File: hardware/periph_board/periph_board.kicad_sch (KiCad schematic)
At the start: 25 parts, among them IC100 CD74HC4067SM96, IC101 LM2937ET-3.3_NOPB, IC102 ADC121S021CIMFX_NOPB, J100 2x10 Male Pins

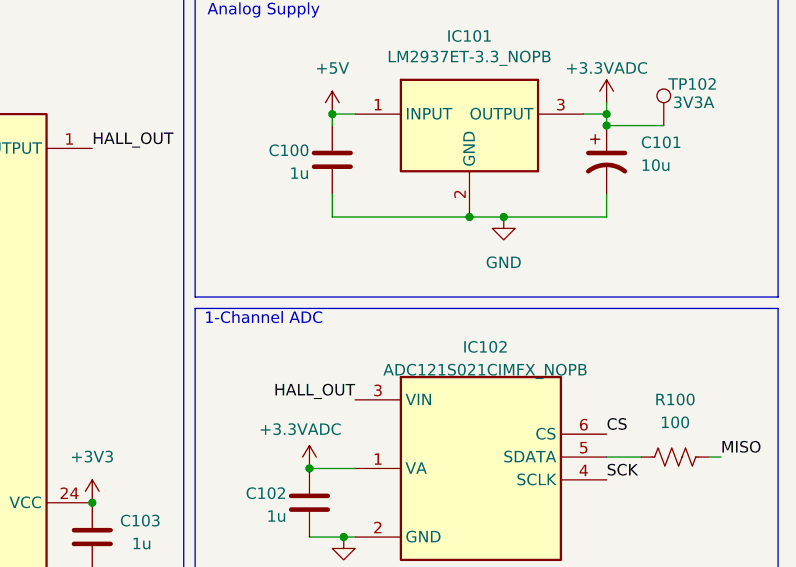
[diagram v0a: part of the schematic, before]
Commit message: fixed sides of peripheral board not being symmetrical. added teardrops. name of board tbd
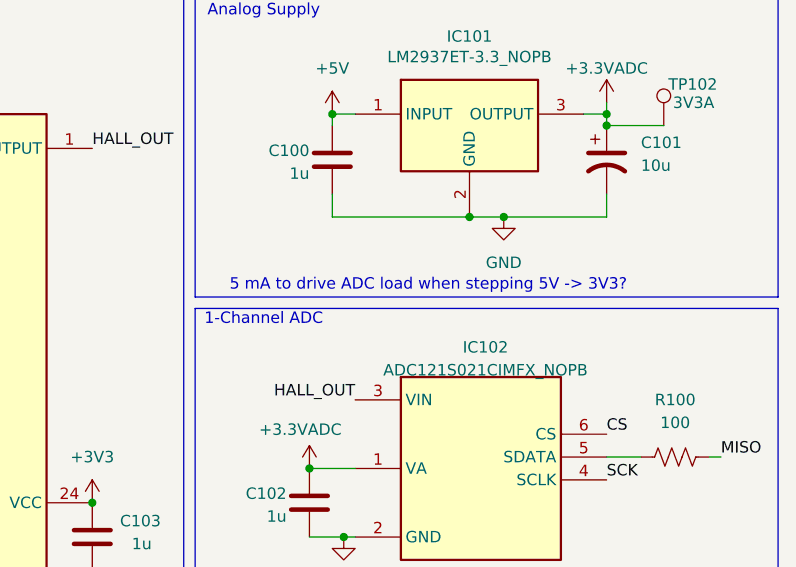
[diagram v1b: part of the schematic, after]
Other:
- note added: "5 mA to drive ADC load when stepping 5V -> 3V3?"
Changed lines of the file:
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@@
+		)
+	)
+	(text "5 mA to drive ADC load when stepping 5V -> 3V3?"
+		(exclude_from_sim no)
+		(at 217.678 46.99 0)
+		(effects
+			(font
+				(size 1.27 1.27)
+			)
 		)
 	)

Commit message: drew schematic
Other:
- note added: "1.2 mA worst case scenario"
- note added: "10 mA worst case scenario"
- note removed: "20 mA worst case scenario"
- note removed: "5 mA to drive ADC load when stepping 5V -> 3V3?"
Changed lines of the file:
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@@
 		)
 	)
-	(text "20 mA worst case scenario"
+	(text "1.2 mA worst case scenario"
 		(exclude_from_sim no)
 		(at 205.74 82.55 0)
@@
 		)
 	)
-	(text "5 mA to drive ADC load when stepping 5V -> 3V3?"
+	(text "10 mA worst case scenario"
 		(exclude_from_sim no)
-		(at 217.678 46.99 0)
+		(at 205.74 47.244 0)
 		(effects
 			(font
@@
 		)
 		(property "Value" "ADC121S021CIMFX_NOPB"
-			(at 224.028 56.388 0)
+			(at 223.52 55.626 0)
 			(effects
 				(font

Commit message: save before nuke SPI ADC
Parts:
- added R200: 3k, Resistor_SMD:R_0805_2012Metric, symbol Device:R_Small_US
- added R201: 3k3, Resistor_SMD:R_0805_2012Metric, symbol Device:R_Small_US
- added R202: 7k5, Resistor_SMD:R_0805_2012Metric, symbol Device:R_Small_US
- added R203: 9k1, Resistor_SMD:R_0805_2012Metric, symbol Device:R_Small_US
- added R204: 1k5, Resistor_SMD:R_0805_2012Metric, symbol Device:R_Small_US
- added R205: 1k3, Resistor_SMD:R_0805_2012Metric, symbol Device:R_Small_US
- added R206: 2k, Resistor_SMD:R_0805_2012Metric, symbol Device:R_Small_US
- added R207: 2k0, Resistor_SMD:R_0805_2012Metric, symbol Device:R_Small_US
- J100: value 2x10 Male Pins -> 2x9 Male Pins; footprint Connector_PinSocket_2.54mm:PinSocket_2x10_P2.54mm_Vertical -> Connector_PinSocket_2.54mm:PinSocket_2x09_P2.54mm_Vertical; symbol Connector_Generic:Conn_02x10_Odd_Even -> Connector_Generic:Conn_02x09_Odd_Even
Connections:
- net +3.3VADC is gone; now on net +3V3: C101.1, C102.2, IC101.3 (OUTPUT), IC102.1 (VA), TP102.1
- net +3V3: now also R200.1, R202.1, R204.1, R205.1; no longer J100.1 (Pin_1), J100.2 (Pin_2)
- net +5V: now also J100.1 (Pin_1), J100.2 (Pin_2); no longer J100.3 (Pin_3), J100.4 (Pin_4)
- net CS: now also J100.7 (Pin_7), J100.8 (Pin_8); no longer J100.10 (Pin_10), J100.9 (Pin_9)
- net GND: now also J100.17 (Pin_17), J100.18 (Pin_18), R201.2, R203.2, R206.2, R207.2; no longer J100.19 (Pin_19), J100.20 (Pin_20)
- net MISO: now also J100.5 (Pin_5), J100.6 (Pin_6); no longer J100.7 (Pin_7), J100.8 (Pin_8)
- net S0: now also J100.10 (Pin_10), J100.9 (Pin_9); no longer J100.11 (Pin_11), J100.12 (Pin_12)
- net S1: now also J100.11 (Pin_11), J100.12 (Pin_12); no longer J100.13 (Pin_13), J100.14 (Pin_14)
- net S2: now also J100.13 (Pin_13), J100.14 (Pin_14); no longer J100.15 (Pin_15), J100.16 (Pin_16)
- net S3: now also J100.15 (Pin_15), J100.16 (Pin_16); no longer J100.17 (Pin_17), J100.18 (Pin_18)
- net SCK: now also J100.3 (Pin_3), J100.4 (Pin_4); no longer J100.5 (Pin_5), J100.6 (Pin_6)
- net 2V000: now reaches IC100.16 (I15)
- net 2V000: now also R205.2, R207.1
- net 1V866: now reaches IC100.17 (I14)
- net 1V866: now also R204.2, R206.1
- net 1V810: now reaches IC100.18 (I13)
- net 1V810: now also R202.2, R203.1
- net 1V729: now reaches IC100.19 (I12)
- net 1V729: now also R200.2, R201.1
- no-connect marks 4 -> 0
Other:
- note added: "Test Voltages"
- moved on the sheet: C100, C101, C102, C103, H100, H101, IC100, IC101, IC102, R100, TP102

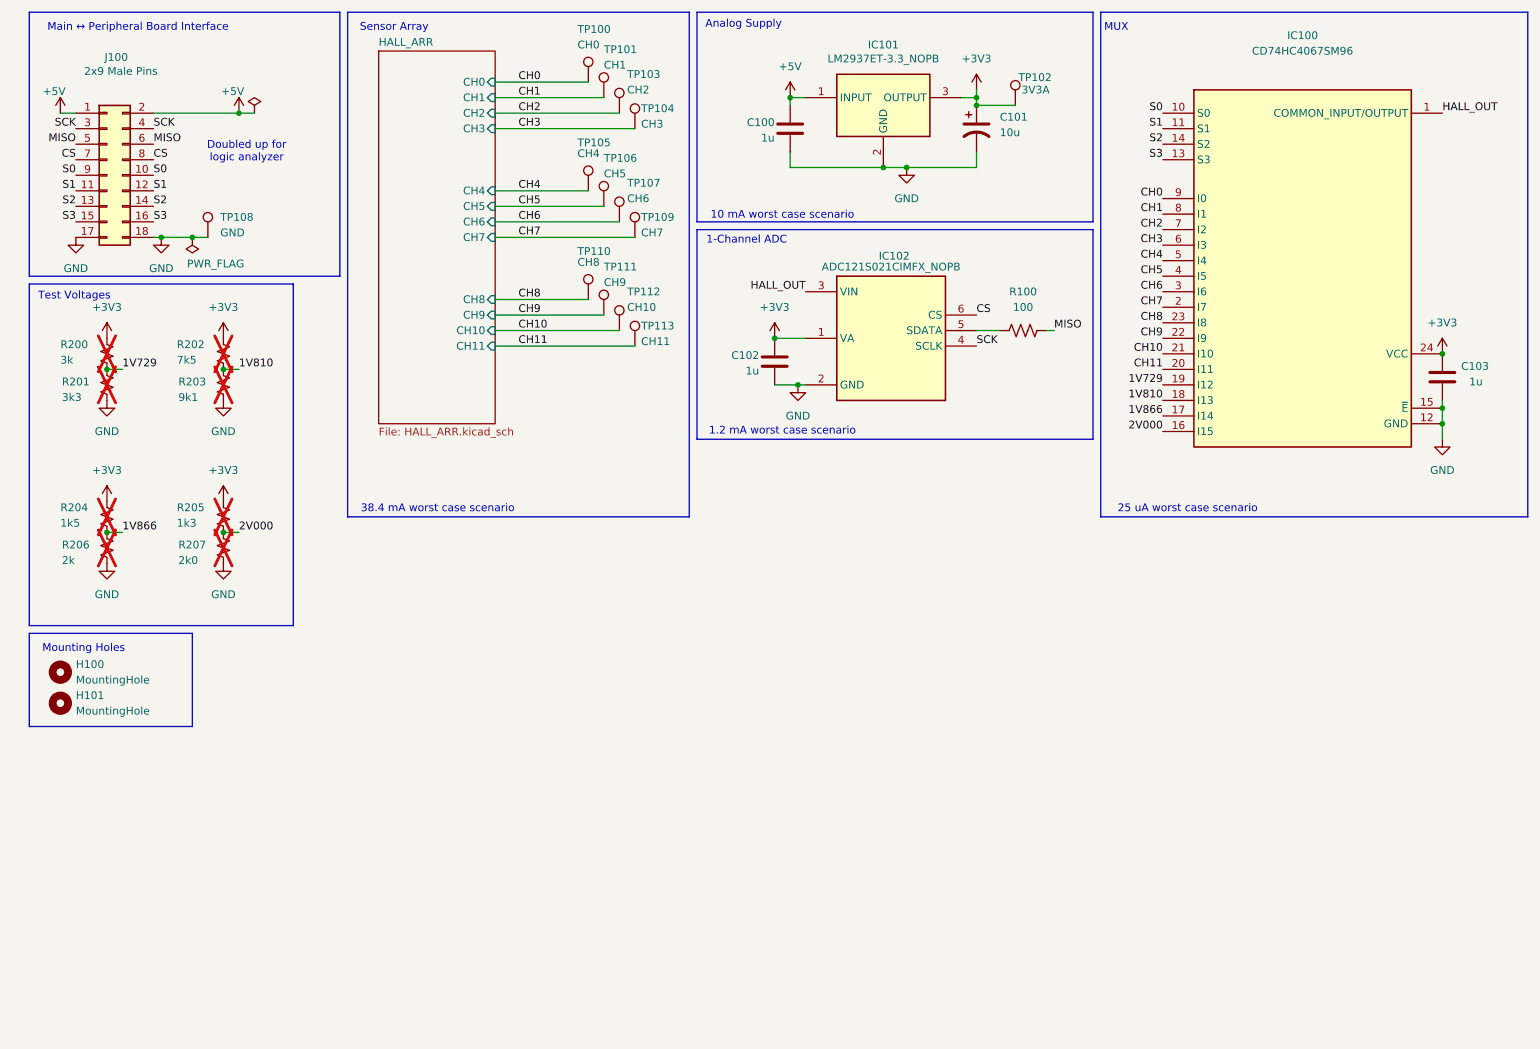
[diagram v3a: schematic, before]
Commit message: port to i2c for both boards. periph board passes drc
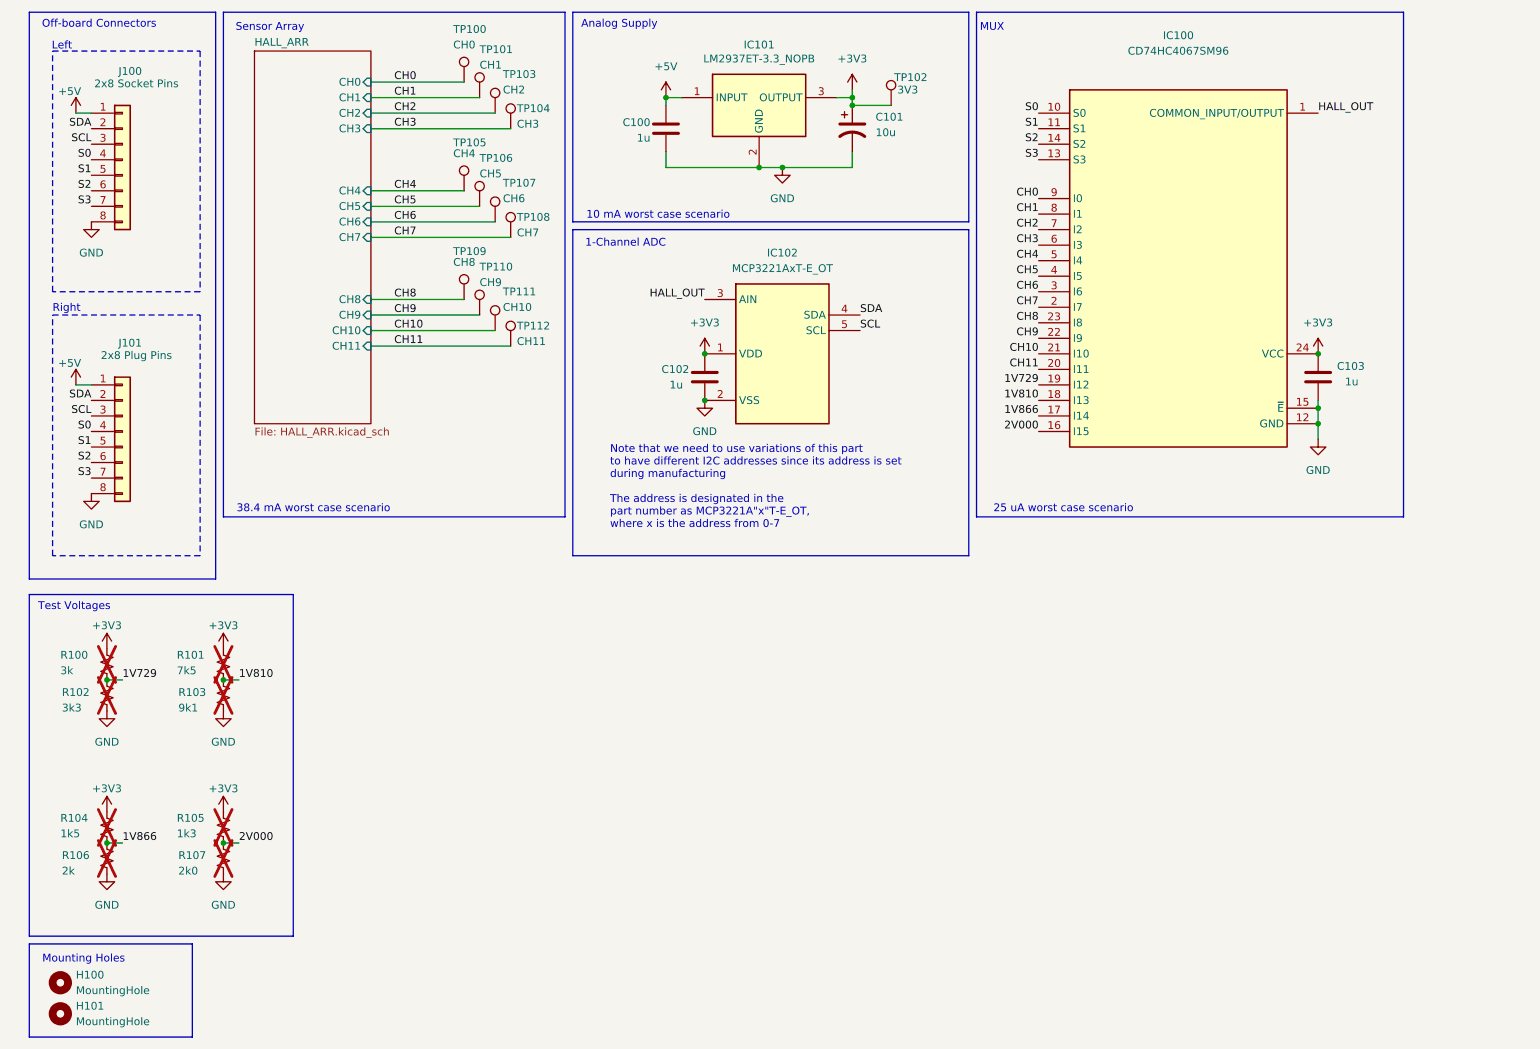
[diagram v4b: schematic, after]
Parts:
- removed IC102: ADC121S021CIMFX_NOPB, SamacSys_Parts:SOT95P280X145-6N, symbol SamacSys_Parts:ADC121S021CIMFX_NOPB
- removed R100: 100, Resistor_SMD:R_0805_2012Metric, symbol Device:R_US
- removed TP108: GND, SamacSys_Parts:bettertestpoint2, symbol Connector:TestPoint
- added IC102: MCP3221AxT-E_OT, SOT95P280X145-5N, symbol SamacSys_Parts:MCP3221A5T-E_OT
- added J101: 2x8 Plug Pins, Connector_PinSocket_2.54mm:PinSocket_1x08_P2.54mm_Vertical, symbol Connector_Generic:Conn_01x08
- C101: footprint Capacitor_SMD:C_0805_2012Metric -> Capacitor_SMD:C_0805_2012Metric_Pad1.18x1.45mm_HandSolder
- J100: value 2x9 Male Pins -> 2x8 Socket Pins; footprint Connector_PinSocket_2.54mm:PinSocket_2x09_P2.54mm_Vertical -> Connector_PinSocket_2.54mm:PinSocket_1x08_P2.54mm_Vertical; symbol Connector_Generic:Conn_02x09_Odd_Even -> Connector_Generic:Conn_01x08
- R100: renamed from R200; footprint Resistor_SMD:R_0805_2012Metric -> Resistor_SMD:R_0805_2012Metric_Pad1.20x1.40mm_HandSolder
- R101: renamed from R202; footprint Resistor_SMD:R_0805_2012Metric -> Resistor_SMD:R_0805_2012Metric_Pad1.20x1.40mm_HandSolder
- R102: renamed from R201; footprint Resistor_SMD:R_0805_2012Metric -> Resistor_SMD:R_0805_2012Metric_Pad1.20x1.40mm_HandSolder
- R103: renamed from R203; footprint Resistor_SMD:R_0805_2012Metric -> Resistor_SMD:R_0805_2012Metric_Pad1.20x1.40mm_HandSolder
- R104: renamed from R204; footprint Resistor_SMD:R_0805_2012Metric -> Resistor_SMD:R_0805_2012Metric_Pad1.20x1.40mm_HandSolder
- R105: renamed from R205; footprint Resistor_SMD:R_0805_2012Metric -> Resistor_SMD:R_0805_2012Metric_Pad1.20x1.40mm_HandSolder
- R106: renamed from R206; footprint Resistor_SMD:R_0805_2012Metric -> Resistor_SMD:R_0805_2012Metric_Pad1.20x1.40mm_HandSolder
- R107: renamed from R207; footprint Resistor_SMD:R_0805_2012Metric -> Resistor_SMD:R_0805_2012Metric_Pad1.20x1.40mm_HandSolder
- TP102: value 3V3A -> 3V3
- renumbered TP109 to TP108, TP110 to TP109, TP111 to TP110, TP112 to TP111, TP113 to TP112
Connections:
- net +3V3: now also IC102.1 (VDD)
- net +5V: now also J101.1 (Pin_1); no longer J100.2 (Pin_2)
- net GND: now also J100.8 (Pin_8), IC102.2 (VSS), J101.8 (Pin_8); no longer J100.17 (Pin_17), J100.18 (Pin_18)
- net HALL_OUT: now also IC102.3 (AIN)
- net S0: now also J100.4 (Pin_4), J101.4 (Pin_4); no longer J100.10 (Pin_10), J100.9 (Pin_9)
- net S1: now also J100.5 (Pin_5), J101.5 (Pin_5); no longer J100.11 (Pin_11), J100.12 (Pin_12)
- net S2: now also J100.6 (Pin_6), J101.6 (Pin_6); no longer J100.13 (Pin_13), J100.14 (Pin_14)
- net S3: now also J100.7 (Pin_7), J101.7 (Pin_7); no longer J100.15 (Pin_15), J100.16 (Pin_16)
- removed net CS: J100.7 (Pin_7), J100.8 (Pin_8)
- removed net MISO: J100.5 (Pin_5), J100.6 (Pin_6)
- net SCK renamed SCL
- net SCL: now also IC102.5 (SCL), J101.3 (Pin_3); no longer J100.4 (Pin_4)
- new net SDA: IC102.4 (SDA), J100.2 (Pin_2), J101.2 (Pin_2)
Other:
- note added: "Left"
- note added: "Note that we need to use variations of this part to have different I2C addresses since its address is set during manufacturing The address is designated in the part number as MCP3221A"x"T-E_OT, where x is the address from 0-7"
- note added: "Off-board Connectors"
- note added: "Right"
- note removed: "1.2 mA worst case scenario"
- note removed: "Doubled up for logic analyzer"
- note removed: "Main ↔ Peripheral Board Interface"
- moved on the sheet: C100, C101, C103, H100, H101, IC100, IC101, R100, R101, R102, R103, R104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
